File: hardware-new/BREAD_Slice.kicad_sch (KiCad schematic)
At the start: 16 parts, among them J1 Conn_01x10_Female, J2 Screw_Terminal_01x02, J3 Screw_Terminal_01x02

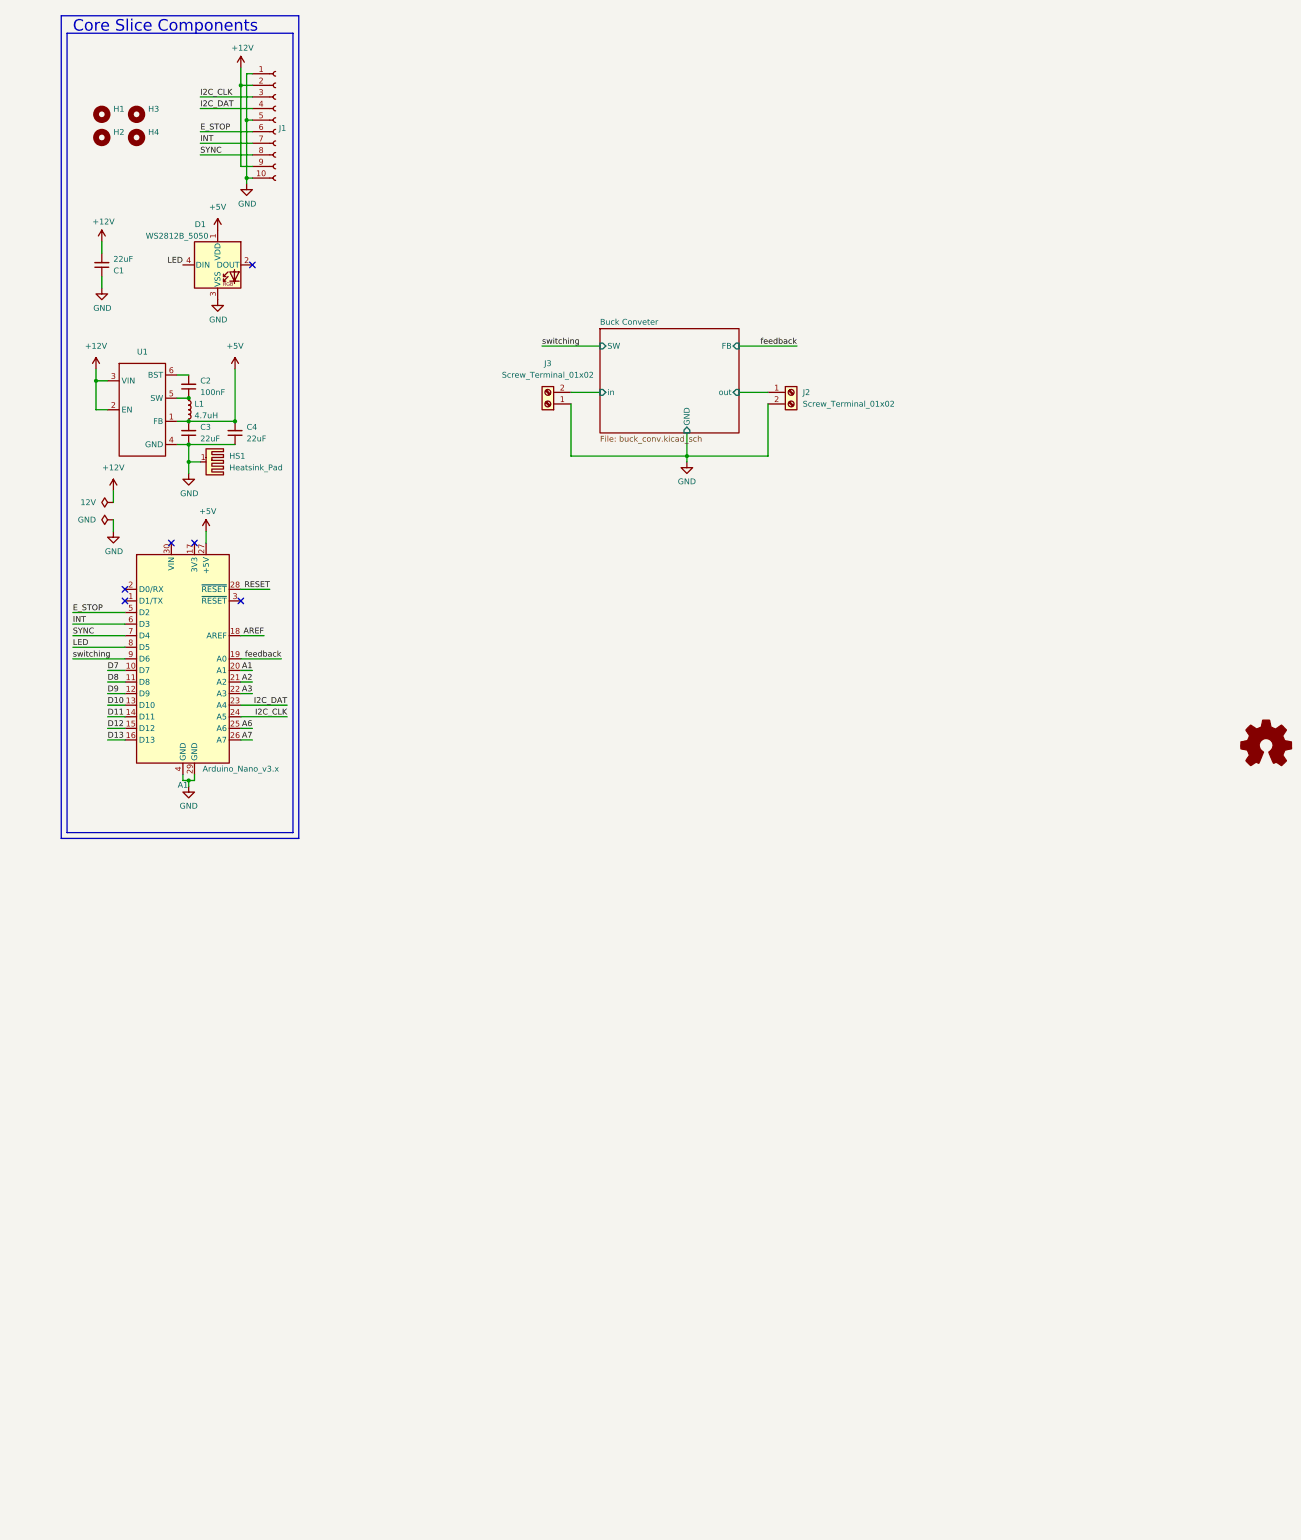
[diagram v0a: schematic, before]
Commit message: finalized to 2L templ
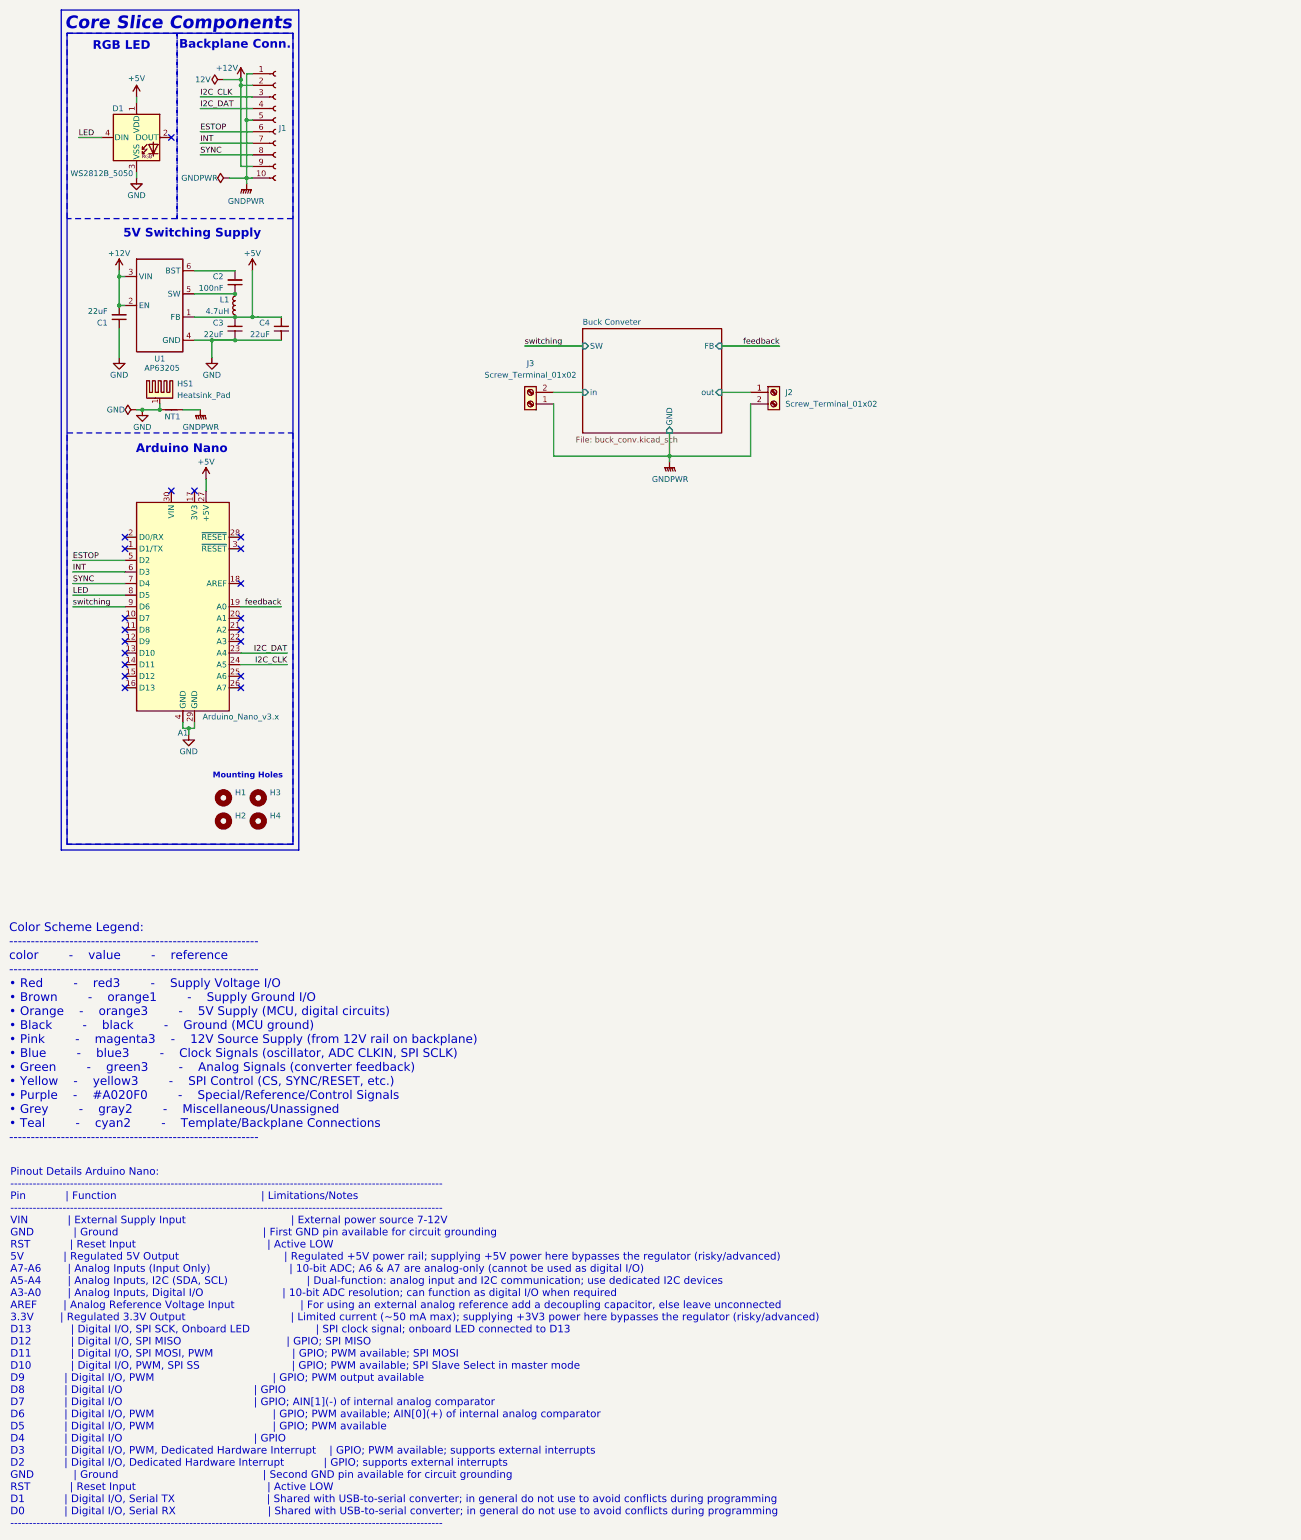
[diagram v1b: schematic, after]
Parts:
- added NT1: NetTie_2, NetTie:NetTie-2_SMD_Pad2.0mm, symbol Device:NetTie_2
- D1: PROD_ID (none) -> DIO-12503
- HS1: footprint KML-Custom:Thermal Pad -> kml-custom:Thermal Pad
- U1: value ~ -> AP63205
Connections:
- net GND: now also NT1.1; no longer J1.1 (Pin_1), J1.10 (Pin_10), J1.5 (Pin_5), J2.2 (Pin_2), J3.1 (Pin_1)
- net A1: no longer names the net of A1.20 (A1)
- net A2: no longer names the net of A1.21 (A2)
- net A3: no longer names the net of A1.22 (A3)
- net A6: no longer names the net of A1.25 (A6)
- net A7: no longer names the net of A1.26 (A7)
- net AREF: no longer names the net of A1.18 (AREF)
- net D10: no longer names the net of A1.13 (D10)
- net D11: no longer names the net of A1.14 (D11)
- net D12: no longer names the net of A1.15 (D12)
- net D13: no longer names the net of A1.16 (D13)
- net D7: no longer names the net of A1.10 (D7)
- net D8: no longer names the net of A1.11 (D8)
- net D9: no longer names the net of A1.12 (D9)
- net E_STOP renamed ESTOP
- net RESET: no longer names the net of A1.28 (~{RESET})
- new net GNDPWR: J1.1 (Pin_1), J1.10 (Pin_10), J1.5 (Pin_5), J2.2 (Pin_2), J3.1 (Pin_1), NT1.2
- no-connect marks 6 -> 20
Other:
- note added: "5V Switching Supply"
- note added: "Arduino Nano"
- note added: "Backplane Conn."
- note added: "Color Scheme Legend: ---------------------------------------------------------- color - value - reference ---------------------------------------------------------- • Red - red3 - Supply Voltage I/O • Brown - orange1 - Supply Ground I/O • Orange - orange3 - 5V Supply (MCU, digital circuits) • Black - black - Ground (MCU ground) • Pink - magenta3 - 12V Source Supply (from 12V rail on backplane) • 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"
- note added: "Mounting Holes"
- note added: "Pinout Details Arduino Nano: -------------------------------------------------------------------------------------------------------------------- Pin | Function | Limitations/Notes -------------------------------------------------------------------------------------------------------------------- VIN | External Supply Input | External power source 7-12V GND | Ground | First GND pin available for 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"
- note added: "RGB LED"
- moved on the sheet: A1, C1, C2, C3, C4, H1, H2, H3, H4, J2, J3, L1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
